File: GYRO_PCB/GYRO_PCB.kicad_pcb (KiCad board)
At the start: 2 copper layers, 74.5 x 84 mm, 18 parts, among them J1 Pmod GYRO, J2 FLASH Socket 1, J3 FLASH Socket 2, J4 Switch Bat, J5 Power Terminal - Raw, U1 NUCLEO64-F446RE

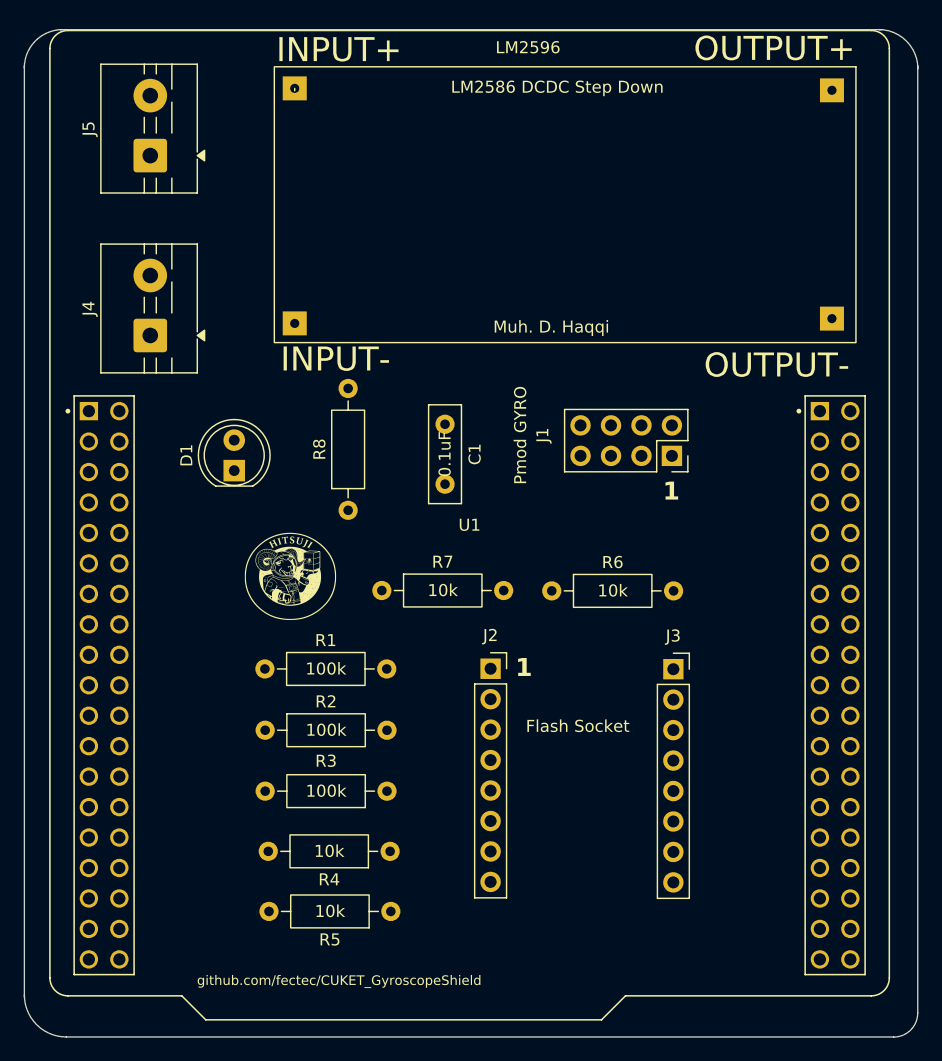
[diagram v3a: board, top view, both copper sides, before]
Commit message: refactor: clean schematic & PCB + feat: add LM2596 & terminal 3D models
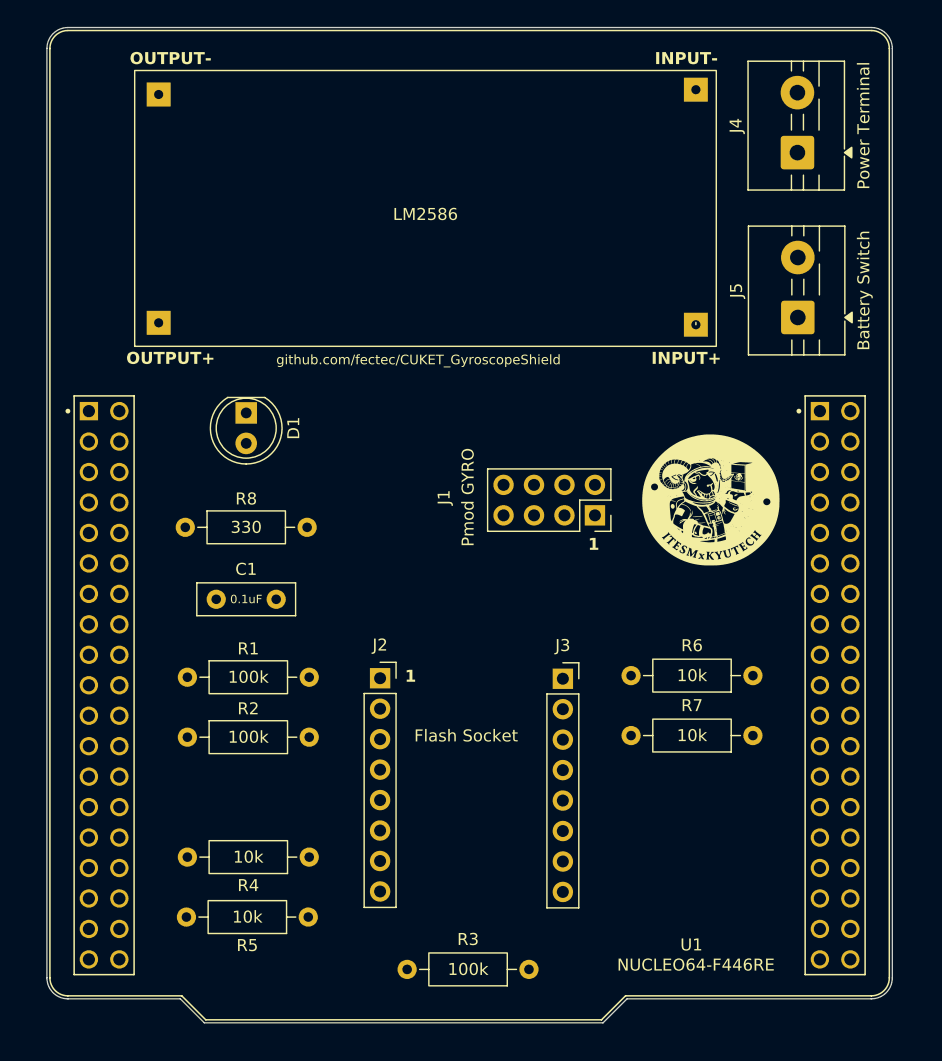
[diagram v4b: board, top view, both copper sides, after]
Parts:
- D1: value SFH4346 -> LED
- J4: renamed from J5; value Power Terminal - Raw -> Power Terminal
- J5: renamed from J4; value Switch Bat -> Battery Switch
- moved J5 54.0 mm to (174.0, 73.5)
- moved J4 54.0 mm to (174.0, 59.8)
- moved LM2596 43.6 mm to (167.2, 75.9), turned to 180 degrees
- moved G*** 35.6 mm to (166.7, 88.7)
- moved R7 33.2 mm to (170.3, 108.4), turned to 180 degrees
- moved C1 24.0 mm to (125.5, 97.0), turned to 0 degrees
- moved R3 19.0 mm to (151.6, 127.9)
- moved R6 18.2 mm to (170.3, 103.4), turned to 180 degrees
- moved R8 13.7 mm to (122.9, 91.0), turned to 0 degrees
- moved J3 9.25 mm to (154.4, 103.6)
- moved J2 9.25 mm to (139.2, 103.6)
- moved J1 8.11 mm to (149.1, 87.0)
- moved R5 6.90 mm to (133.2, 123.5)
- moved R4 6.76 mm to (133.3, 118.5)
- moved R2 6.51 mm to (123.1, 108.5)
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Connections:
- U1 pad CN10_20: unconnected-(U1-GND-PadCN10_20) -> GND
- U1 pad CN10_9: unconnected-(U1-GND-PadCN10_9) -> GND
- U1 pad CN7_19: unconnected-(U1-GND-PadCN7_19) -> GND
- U1 pad CN7_20: unconnected-(U1-GND-PadCN7_20) -> GND
- U1 pad CN7_22: unconnected-(U1-GND-PadCN7_22) -> GND
- U1 pad CN7_8: unconnected-(U1-GND-PadCN7_8) -> GND
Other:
- board size 74.5 x 84 mm -> 70.5 x 83 mm

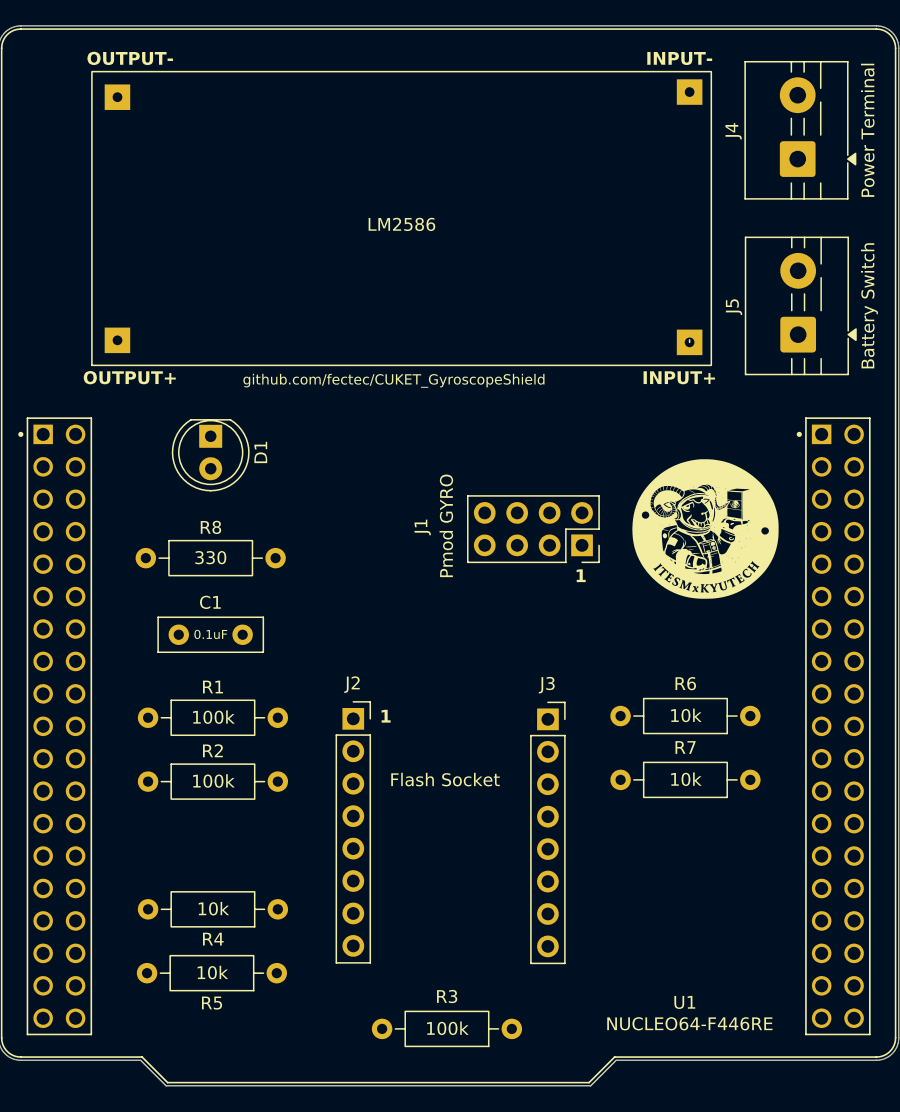
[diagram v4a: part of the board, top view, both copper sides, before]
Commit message: fix: correct DRC & add mechanical limits to gyroscope
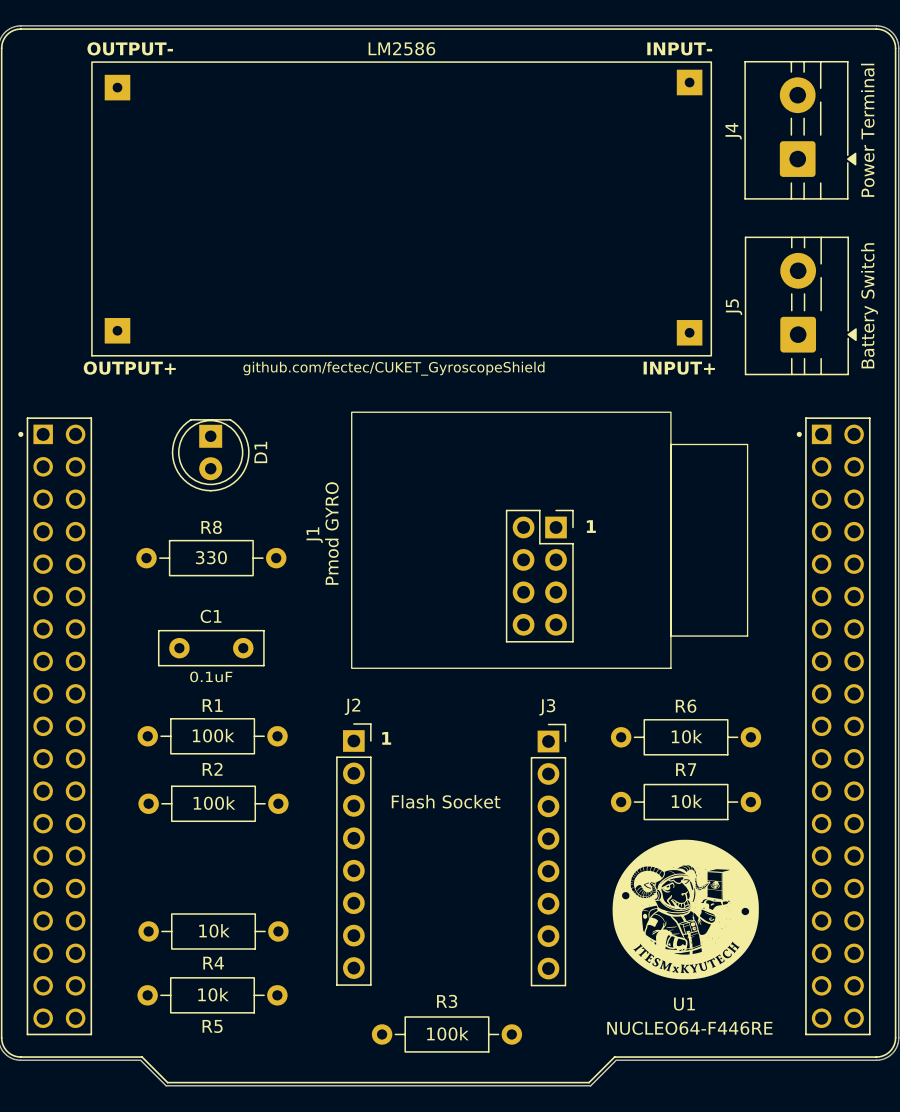
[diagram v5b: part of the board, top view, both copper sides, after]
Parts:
- moved G*** 29.8 mm to (165.2, 118.5)
- moved J1 10.0 mm to (152.0, 96.6), turned to 180 degrees
- moved J2 1.74 mm to (139.2, 105.3)
- moved R4 1.74 mm to (133.3, 120.2)
- moved R7 1.74 mm to (170.3, 110.1)
- moved R2 1.74 mm to (123.1, 110.2)
- moved J3 1.74 mm to (154.4, 105.4)
- moved R5 1.74 mm to (133.2, 125.2)
- moved R6 1.67 mm to (170.3, 105.0)
- moved R1 1.45 mm to (123.1, 105.0)
- moved C1 1.05 mm to (125.5, 98.0)
- moved LM2596 0.75 mm to (167.2, 75.2)
- moved R3 0.44 mm to (151.6, 128.3)
